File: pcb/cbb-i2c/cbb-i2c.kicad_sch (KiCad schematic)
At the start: 22 parts, among them J1 Conn_02x04_Odd_Even, J14 Screw_Terminal_01x08, J2 Screw_Terminal_01x04, J3 Screw_Terminal_01x06, J4 Screw_Terminal_01x06, J5 Conn_01x04, J6 Conn_01x04, U1 MCP23017_SS

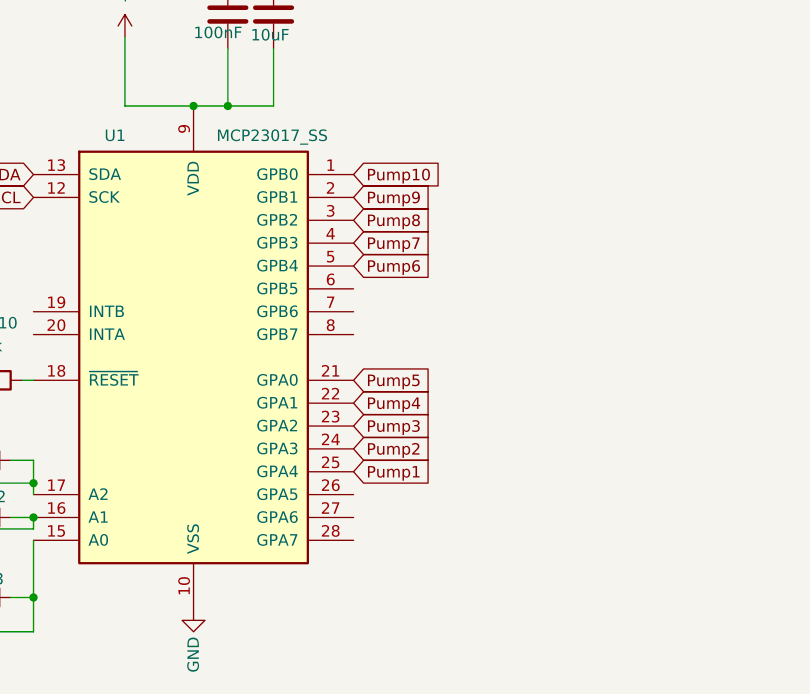
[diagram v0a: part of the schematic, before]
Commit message: adjust mcp routing
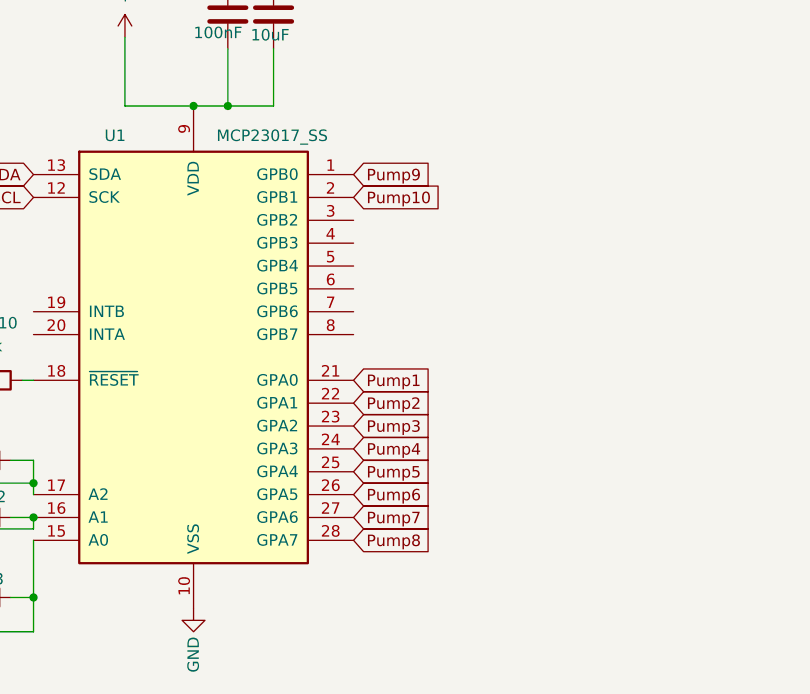
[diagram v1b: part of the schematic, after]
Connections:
- net Pump1: now also U1.21 (GPA0); no longer U1.25 (GPA4)
- net Pump10: now also U1.2 (GPB1); no longer U1.1 (GPB0)
- net Pump2: now also U1.22 (GPA1); no longer U1.24 (GPA3)
- net Pump4: now also U1.24 (GPA3); no longer U1.22 (GPA1)
- net Pump5: now also U1.25 (GPA4); no longer U1.21 (GPA0)
- net Pump6: now also U1.26 (GPA5); no longer U1.5 (GPB4)
- net Pump7: now also U1.27 (GPA6); no longer U1.4 (GPB3)
- net Pump8: now also U1.28 (GPA7); no longer U1.3 (GPB2)
- net Pump9: now also U1.1 (GPB0); no longer U1.2 (GPB1)

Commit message: use 0402 instead 0603 for mcp r
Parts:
- R10k10, R10k11, R10k12, R10k13: MPN C25804 -> C25744
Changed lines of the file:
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@@
 			)
 		)
-		(property "MPN" "C25804"
+		(property "MPN" "C25744"
 			(at 57.15 142.24 0)
 			(effects
@@
 			)
 		)
-		(property "MPN" "C25804"
+		(property "MPN" "C25744"
 			(at 57.15 157.48 0)
 			(effects
@@
 			)
 		)
-		(property "MPN" "C25804"
+		(property "MPN" "C25744"
 			(at 57.15 148.59 0)
 			(effects
@@
 			)
 		)
-		(property "MPN" "C25804"
+		(property "MPN" "C25744"
 			(at 58.42 133.35 0)
 			(effects

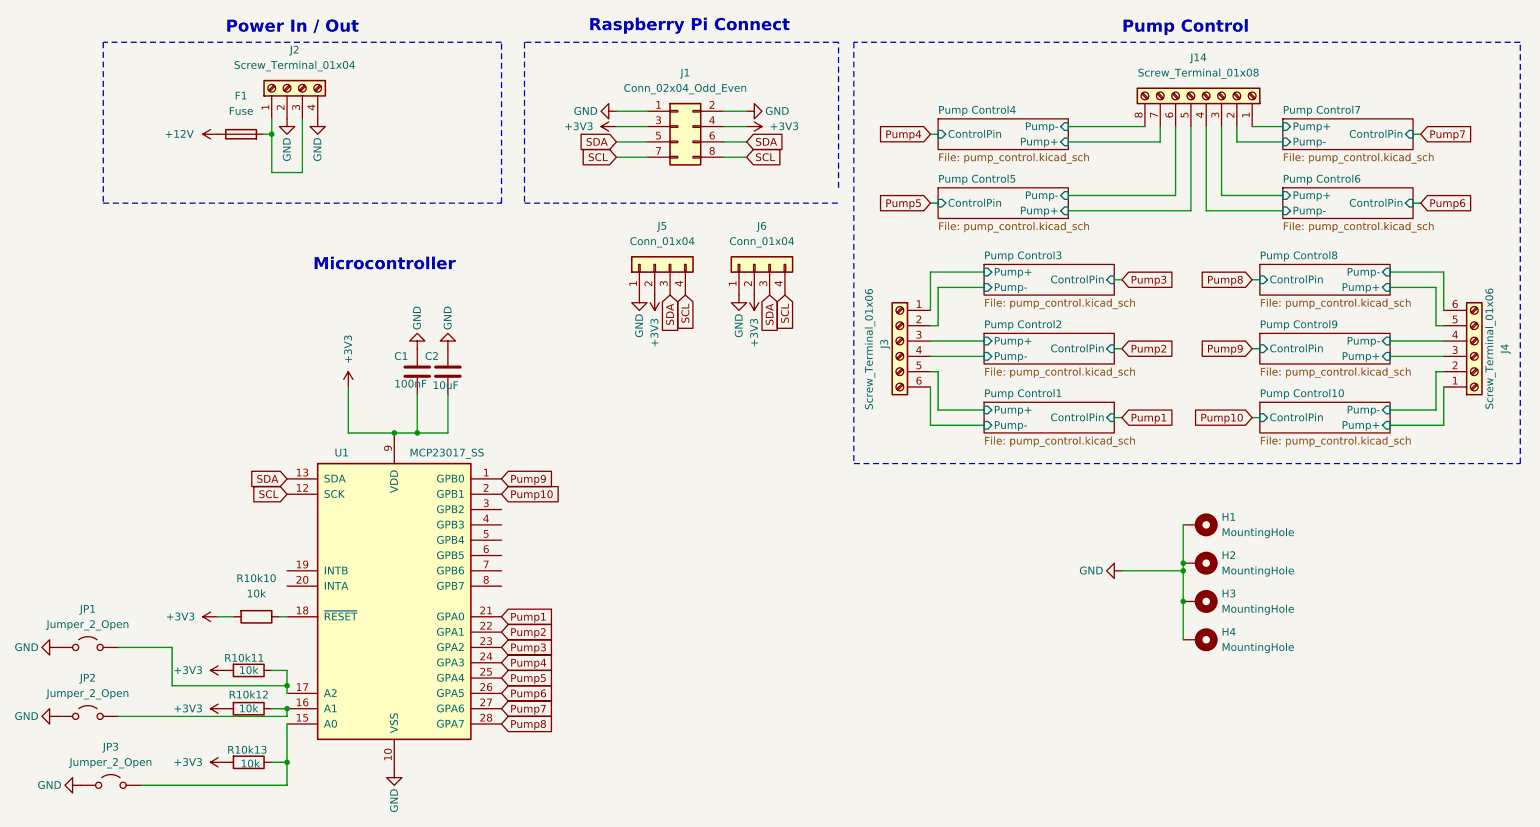
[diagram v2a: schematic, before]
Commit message: adjust cbb-i2c
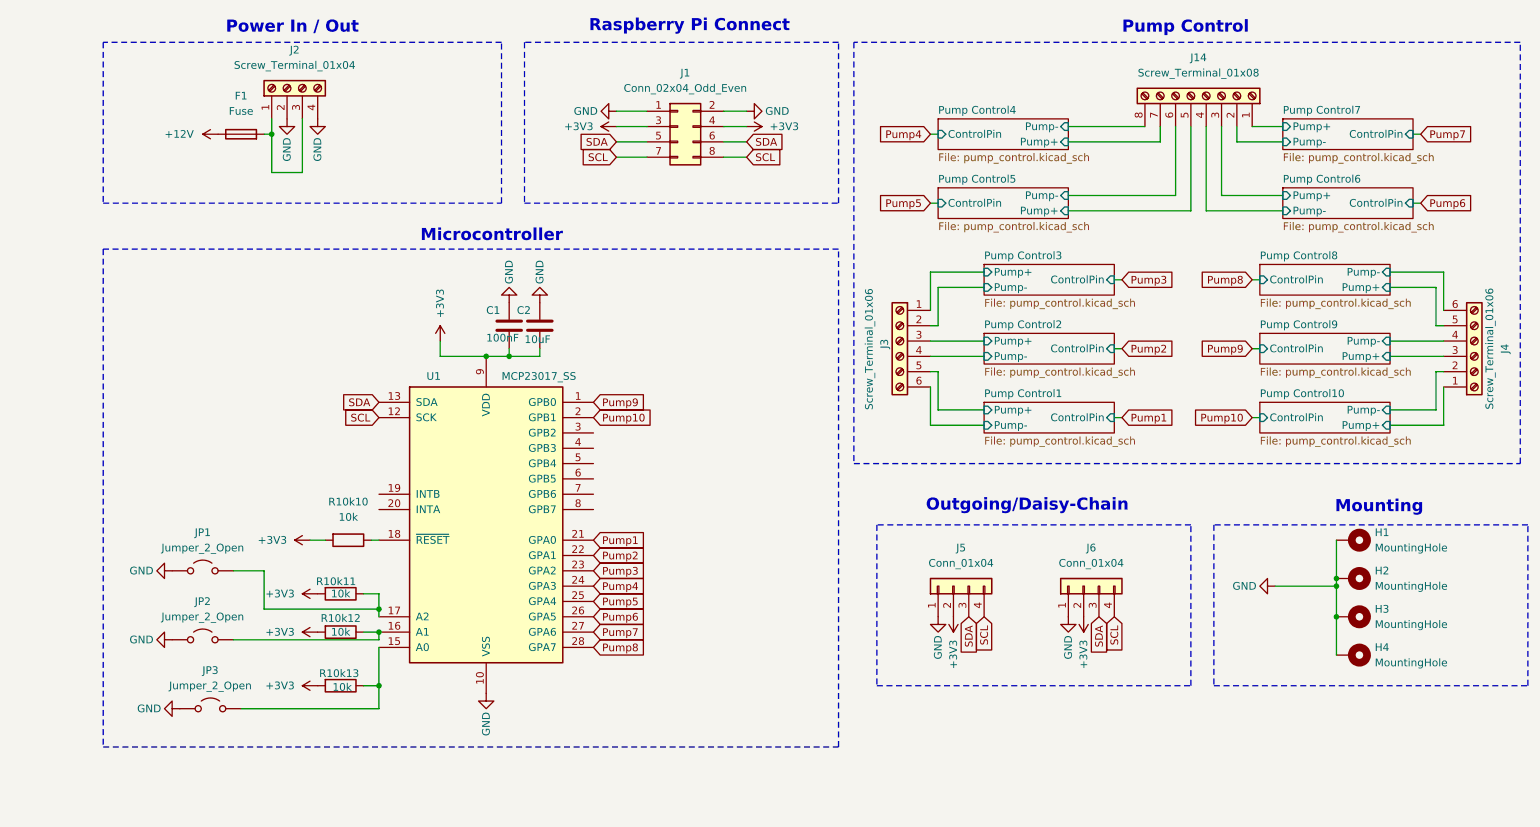
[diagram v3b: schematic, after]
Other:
- note added: "Mounting"
- note added: "Outgoing/Daisy-Chain"
- moved on the sheet: C1, C2, H1, H2, H3, H4, J5, J6, JP1, JP2, JP3, R10k10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

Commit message: add power indicator led to cbb i2c
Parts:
- added D21: LED, LED_SMD:LED_0603_1608Metric, symbol Device:LED
- added R22: 820, Resistor_SMD:R_0603_1608Metric, symbol Device:R
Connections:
- net +3V3: now also R22.2
- net GND: now also D21.1 (K)
- new net: D21.2 (A), R22.1
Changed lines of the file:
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@@
 	)
 	(junction
+		(at 105.41 90.17)
+		(diameter 0)
+		(color 0 0 0 0)
+	)
+	(junction
 		(at 78.74 135.89)
 		(diameter 0)
@@
 		)
 	)
+	(wire
+		(pts
+			(xy 118.11 90.17) (xy 115.57 90.17)
+		)
+		(stroke
+			(width 0)
+			(type default)
+		)
+	)
 	(polyline
 		(pts
@@
 	(wire
 		(pts
+			(xy 105.41 90.17) (xy 107.95 90.17)
+		)
+		(stroke
+			(width 0)
+			(type default)
+		)
+	)
+	(wire
+		(pts
 			(xy 60.96 50.8) (xy 60.96 53.34)
 		)
@@
 	)
 	(symbol
+		(lib_id "Device:R")
+		(at 111.76 90.17 270)
+		(unit 1)
+		(exclude_from_sim no)
+		(in_bom yes)
+		(on_board yes)
+		(dnp no)
+		(property "Reference" "R22"
+			(at 109.982 87.376 90)
+			(effects
+				(font
+					(size 1.27 1.27)
+				)
+				(justify left)
+			)
+		)
+		(property "Value" "820"
+			(at 109.982 90.17 90)
+			(effects
+				(font
+					(size 1.27 1.27)
+				)
+				(justify left)
+			)
+		)
+		(property "Footprint" "Resistor_SMD:R_0603_1608Metric"
+			(at 111.76 88.392 90)
+			(effects
+				(font
+					(size 1.27 1.27)
+				)
+				(hide yes)
+			)
+		)
+		(property "Datasheet" "~"
+			(at 111.76 90.17 0)
+			(effects
+				(font
+					(size 1.27 1.27)
+				)
+				(hide yes)
+			)
+		)
+		(property "Description" ""
+			(at 111.76 90.17 0)
+			(effects
+				(font
+					(size 1.27 1.27)
+				)
+				(hide yes)
+			)
+		)
+		(property "MPN" "C23253"
+			(at 111.76 90.17 90)
+			(effects
+				(font
+					(size 1.27 1.27)
+				)
+				(hide yes)
+			)
+		)
+		(pin "1"
+		)
+		(pin "2"
+		)
+		(instances
+			(project "cbb-i2c"
+				(path "/5575e3e9-07ff-42ca-b261-f5e11b540bc9"
+					(reference "R22")
+					(unit 1)
+				)
+			)
+		)
+	)
+	(symbol
 		(lib_id "power:GND")
 		(at 63.5 50.8 0)
@@
 	(symbol
 		(lib_id "power:GND")
+		(at 118.11 82.55 180)
+		(unit 1)
+		(exclude_from_sim no)
+		(in_bom yes)
+		(on_board yes)
+		(dnp no)
+		(property "Reference" "#PWR020"
+			(at 118.11 76.2 0)
+			(effects
+				(font
+					(size 1.27 1.27)
+				)
+				(hide yes)
+			)
+		)
+		(property "Value" "GND"
+			(at 118.11 77.47 90)
+			(effects
+				(font
+					(size 1.27 1.27)
+				)
+			)
+		)
+		(property "Footprint" ""
+			(at 118.11 82.55 0)
+			(effects
+				(font
+					(size 1.27 1.27)
+				)
+				(hide yes)
+			)
+		)
+		(property "Datasheet" ""
+			(at 118.11 82.55 0)
+			(effects
+				(font
+					(size 1.27 1.27)
+				)
+				(hide yes)
+			)
+		)
+		(property "Description" ""
+			(at 118.11 82.55 0)
+			(effects
+				(font
+					(size 1.27 1.27)
+				)
+				(hide yes)
+			)
+		)
+		(pin "1"
+		)
+		(instances
+			(project "cbb-i2c"
+				(path "/5575e3e9-07ff-42ca-b261-f5e11b540bc9"
+					(reference "#PWR020")
+					(unit 1)
+				)
+			)
+		)
+	)
+	(symbol
+		(lib_id "power:GND")
 		(at 105.41 81.28 180)
 		(unit 1)
@@
 					(unit 1)
 				)
+			)
+		)
+	)
+	(symbol
+		(lib_id "Device:LED")
+		(at 118.11 86.36 270)
+		(unit 1)
+		(exclude_from_sim no)
+		(in_bom yes)
+		(on_board yes)
+		(dnp no)
+		(fields_autoplaced yes)
+		(property "Reference" "D21"
+			(at 120.65 83.5024 90)
+			(effects
+				(font
+					(size 1.27 1.27)
+				)
+				(justify left)
+			)
+		)
+		(property "Value" "LED"
+			(at 120.65 86.0424 90)
+			(effects
+				(font
+					(size 1.27 1.27)
+				)
+				(justify left)
+			)
+		)
+		(property "Footprint" "LED_SMD:LED_0603_1608Metric"
+			(at 118.11 86.36 0)
+			(effects
+				(font
+					(size 1.27 1.27)
+				)
+				(hide yes)
+			)
+		)
+		(property "Datasheet" "~"
+			(at 118.11 86.36 0)
+			(effects
+				(font
+					(size 1.27 1.27)
+				)
+				(hide yes)
+			)
+		)
+		(property "Description" ""
+			(at 118.11 86.36 0)
+			(effects
+				(font
+					(size 1.27 1.27)
+				)
+				(hide yes)
+			)
+		)
+		(property "MPN" "C2286"
+			(at 118.11 86.36 0)
+			(effects
+				(font
+					(size 1.27 1.27)
+				)
+				(hide yes)
+			)
+		)
+		(pin "1"
+		)
+		(pin "2"
+		)
+		(instances
+			(project "cbb-i2c"
+				(path "/5575e3e9-07ff-42ca-b261-f5e11b540bc9"
+					(reference "D21")
+					(unit 1)
+				)
